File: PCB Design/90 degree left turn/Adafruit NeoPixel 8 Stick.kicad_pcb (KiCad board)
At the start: 2 copper layers, 24.6 x 23.9 mm, 5 parts, among them CN1 1X4SMT, CN2 1X4SMT

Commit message: arrows
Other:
- board text removed: "DIN"
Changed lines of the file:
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@@
       (net 2 "GND") (pinfunction "4") (pintype "bidirectional") (solder_mask_margin 0.1016))
   )
+  (gr_line (start 132.08 105.918) (end 138.684 99.06) (layer "B.SilkS") (width 0.12))
+  (gr_line (start 135.89 99.06) (end 138.684 99.06) (layer "B.SilkS") (width 0.12))
+  (gr_line (start 138.684 99.06) (end 138.684 101.6) (layer "B.SilkS") (width 0.12))
   (gr_line (start 131.064 113.792) (end 122.428 113.792) (layer "Edge.Cuts") (width 0.05))
   (gr_line (start 131.064 98.552) (end 131.064 89.916) (layer "Edge.Cuts") (width 0.05))
@@
     (effects (font (size 1.143 1.143) (thickness 0.127)) (justify left bottom mirror))
   )
-  (gr_text "4-7VDC" (at 128.9812 107.0864) (layer "B.SilkS")
-    (effects (font (size 1.143 1.143) (thickness 0.127)) (justify right top mirror))
-  )
   (gr_text "DOUT" (at 155.194 131.4704 270) (layer "B.SilkS")
     (effects (font (size 1.143 1.143) (thickness 0.127)) (justify left bottom mirror))
@@
     (effects (font (size 1.143 1.143) (thickness 0.127)) (justify left bottom mirror))
   )
-  (gr_text "DIN" (at 128.9812 105.0544) (layer "B.SilkS")
-    (effects (font (size 1.143 1.143) (thickness 0.127)) (justify right top mirror))
-  )
   (gr_text "GND" (at 157.734 131.4704 270) (layer "B.SilkS")
     (effects (font (size 1.143 1.143) (thickness 0.127)) (justify left bottom mirror))
   )
-  (gr_text "GND" (at 128.9812 102.5144) (layer "B.SilkS")
-    (effects (font (size 1.143 1.143) (thickness 0.127)) (justify right top mirror))
-  )
-  (gr_text "GND" (at 128.9812 109.1184) (layer "B.SilkS")
-    (effects (font (size 1.143 1.143) (thickness 0.127)) (justify right top mirror))
-  )
   (segment (start 129.958 108.026) (end 134.421993 108.026) (width 0.25) (layer "F.Cu") (net 1))

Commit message: 6 pin
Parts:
- moved CN1 2.54 mm to (141.0, 94.4)
- moved D1 1.83 mm to (126.5, 108.0)
- moved D3 1.70 mm to (140.7, 94.0)
- moved D2 1.63 mm to (134.6, 102.1)
- moved CN2 0.52 mm to (126.9, 107.4)
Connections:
- CN1 pad 1: GND -> Net-(CN1-Pad1)
- CN1 pad 3: +5V -> GND
- CN1 pad 4: GND -> Net-(D3-Pad2)
- D3 pad 2: Net-(CN1-Pad2) -> Net-(D3-Pad2)
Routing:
- net Net-(CN1-Pad2): track 0.00 -> 14.4 mm, vias 1 -> 0
- net Net-(CN1-Pad1): track 0.00 -> 9.51 mm
- net +5V: track 28.9 -> 35.1 mm
- net Net-(CN2-Pad3): track 3.97 -> 0.00 mm
- net Net-(D3-Pad2): track 0.00 -> 3.78 mm, vias 0 -> 1
- net Net-(D2-Pad2): track 5.57 -> 8.26 mm
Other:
- board size 24.6 x 23.9 mm -> 28.6 x 28.6 mm
- board text removed: "4-7VDC"
- board text removed: "DOUT"
- board text removed: "GND"

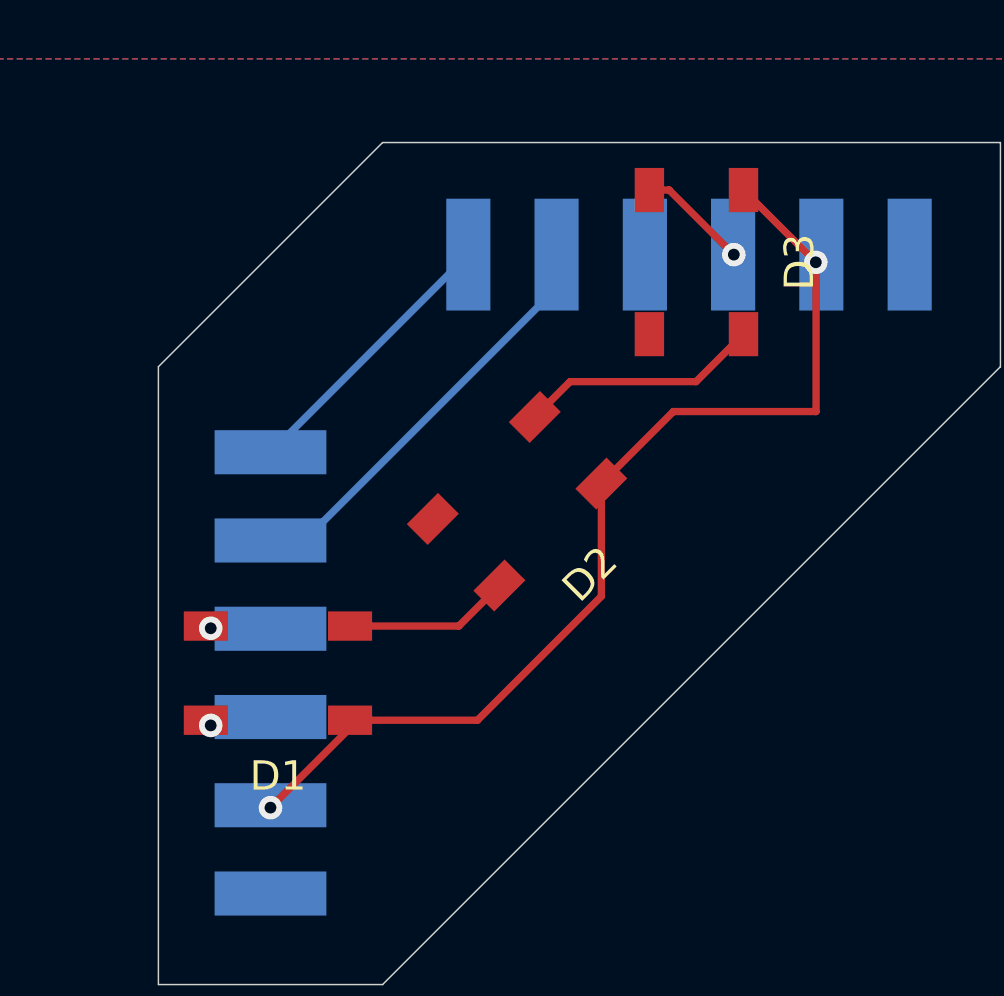
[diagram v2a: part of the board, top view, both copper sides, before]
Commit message: move vias off pads
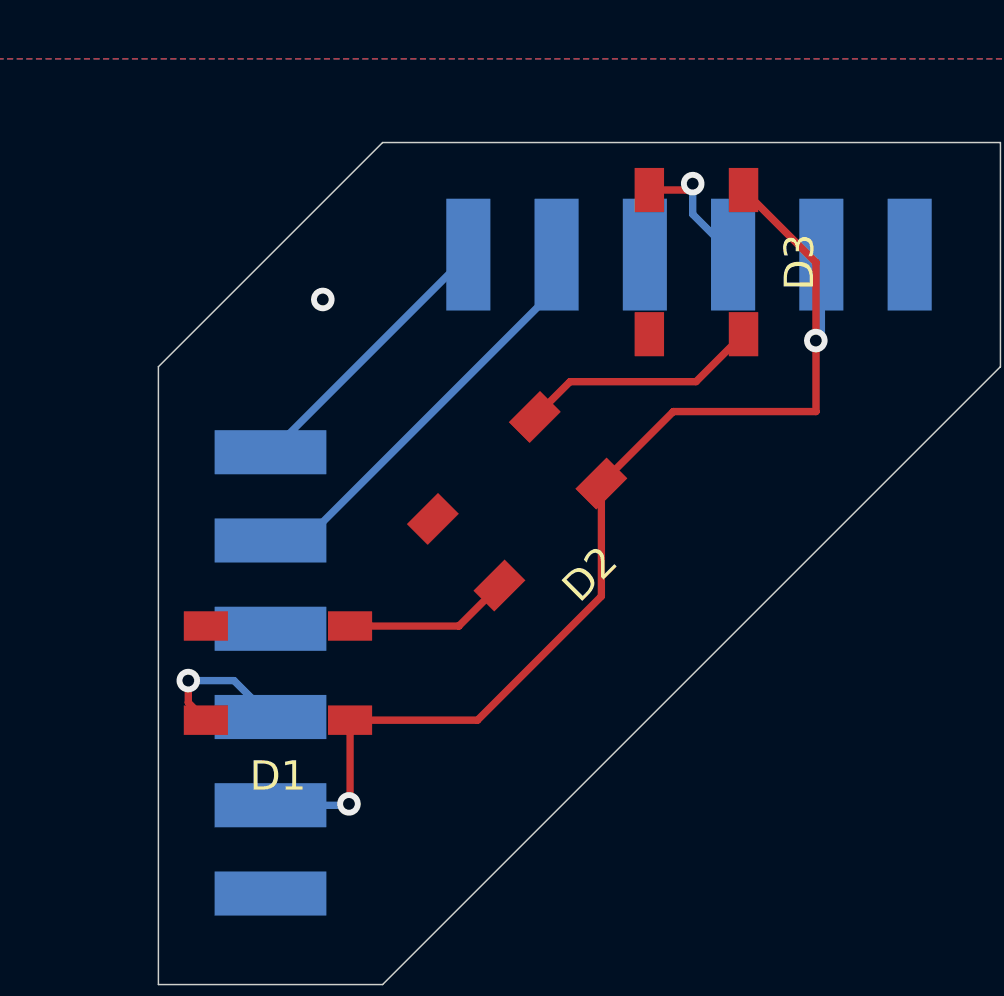
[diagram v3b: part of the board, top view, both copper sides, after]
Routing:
- net Net-(CN2-Pad3): track 0.00 -> 4.90 mm
- net +5V: track 35.1 -> 39.5 mm
- net Net-(D3-Pad2): track 3.78 -> 4.54 mm
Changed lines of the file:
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@@
   (segment (start 144.78 93.994) (end 144.773 93.987) (width 0.25) (layer "F.Cu") (net 1))
   (segment (start 133.274 109.55) (end 137.483782 105.340218) (width 0.25) (layer "F.Cu") (net 1))
-  (segment (start 128.942 109.818) (end 128.942 109.55) (width 0.25) (layer "F.Cu") (net 1))
   (segment (start 128.942 109.55) (end 133.274 109.55) (width 0.25) (layer "F.Cu") (net 1))
   (segment (start 137.483782 105.340218) (end 137.483782 101.506959) (width 0.25) (layer "F.Cu") (net 1))
-  (segment (start 126.238 112.522) (end 128.942 109.818) (width 0.25) (layer "F.Cu") (net 1))
-  (via (at 126.238 112.522) (size 0.8) (drill 0.4) (layers "F.Cu" "B.Cu") (net 1))
-  (via (at 144.773 93.987) (size 0.8) (drill 0.4) (layers "F.Cu" "B.Cu") (net 1))
-  (via (at 124.206 106.426) (size 0.8) (drill 0.4) (layers "F.Cu" "B.Cu") (net 2))
+  (segment (start 128.942 109.55) (end 128.942 112.358) (width 0.25) (layer "F.Cu") (net 1))
+  (segment (start 128.942 112.358) (end 128.905 112.395) (width 0.25) (layer "F.Cu") (net 1))
+  (via (at 128.905 112.395) (size 0.8) (drill 0.4) (layers "F.Cu" "B.Cu") (net 1))
+  (via (at 144.773 96.647) (size 0.8) (drill 0.4) (layers "F.Cu" "B.Cu") (net 1))
+  (segment (start 144.962 96.458) (end 144.773 96.647) (width 0.25) (layer "B.Cu") (net 1))
+  (segment (start 128.858 112.442) (end 128.905 112.395) (width 0.25) (layer "B.Cu") (net 1))
+  (segment (start 144.962 93.725998) (end 144.962 96.458) (width 0.25) (layer "B.Cu") (net 1))
+  (segment (start 126.238 112.442) (end 128.858 112.442) (width 0.25) (layer "B.Cu") (net 1))
+  (via (at 128.016 95.25) (size 0.8) (drill 0.4) (layers "F.Cu" "B.Cu") (free) (net 2))
   (segment (start 135.962 94.868) (end 135.962 93.725998) (width 0.25) (layer "B.Cu") (net 3))
   (segment (start 127.388 103.442) (end 135.962 94.868) (width 0.25) (layer "B.Cu") (net 3))
   (segment (start 126.238 103.442) (end 127.388 103.442) (width 0.25) (layer "B.Cu") (net 3))
-  (via (at 124.206 109.728) (size 0.8) (drill 0.4) (layers "F.Cu" "B.Cu") (net 4))
+  (segment (start 123.444 108.204) (end 123.444 108.952) (width 0.25) (layer "F.Cu") (net 4))
+  (segment (start 123.444 108.952) (end 124.042 109.55) (width 0.25) (layer "F.Cu") (net 4))
+  (via (at 123.444 108.204) (size 0.8) (drill 0.4) (layers "F.Cu" "B.Cu") (net 4))
+  (segment (start 123.444 108.204) (end 125 108.204) (width 0.25) (layer "B.Cu") (net 4))
+  (segment (start 125 108.204) (end 126.238 109.442) (width 0.25) (layer "B.Cu") (net 4))
   (segment (start 128.942 106.35) (end 132.640741 106.35) (width 0.25) (layer "F.Cu") (net 5))
   (segment (start 132.640741 106.35) (end 134.018959 104.971782) (width 0.25) (layer "F.Cu") (net 5))
@@
   (segment (start 140.702 98.044) (end 142.316 96.43) (width 0.25) (layer "F.Cu") (net 6))
   (segment (start 136.421259 98.044) (end 140.702 98.044) (width 0.25) (layer "F.Cu") (net 6))
-  (segment (start 141.986 93.726) (end 139.79 91.53) (width 0.25) (layer "F.Cu") (net 7))
-  (segment (start 139.79 91.53) (end 139.116 91.53) (width 0.25) (layer "F.Cu") (net 7))
-  (via (at 141.986 93.726) (size 0.8) (drill 0.4) (layers "F.Cu" "B.Cu") (net 7))
+  (segment (start 139.116 91.53) (end 140.372 91.53) (width 0.25) (layer "F.Cu") (net 7))
+  (segment (start 140.372 91.53) (end 140.589 91.313) (width 0.25) (layer "F.Cu") (net 7))
+  (via (at 140.589 91.313) (size 0.8) (drill 0.4) (layers "F.Cu" "B.Cu") (net 7))
+  (segment (start 140.589 91.313) (end 140.589 92.352998) (width 0.25) (layer "B.Cu") (net 7))
+  (segment (start 140.589 92.352998) (end 141.962 93.725998) (width 0.25) (layer "B.Cu") (net 7))
   (segment (start 126.245998 100.442) (end 132.962 93.725998) (width 0.25) (layer "B.Cu") (net 8))
   (segment (start 126.238 100.442) (end 126.245998 100.442) (width 0.25) (layer "B.Cu") (net 8))
